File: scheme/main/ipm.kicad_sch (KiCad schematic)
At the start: 2 parts

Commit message: sheets titles
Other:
- title: (none) -> Силовой модуль
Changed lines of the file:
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@@
 	(generator_version "8.0")
 	(paper "A3")
+	(title_block
+		(title "Силовой модуль")
+	)
 	(junction
 		(at 205.74 96.52)

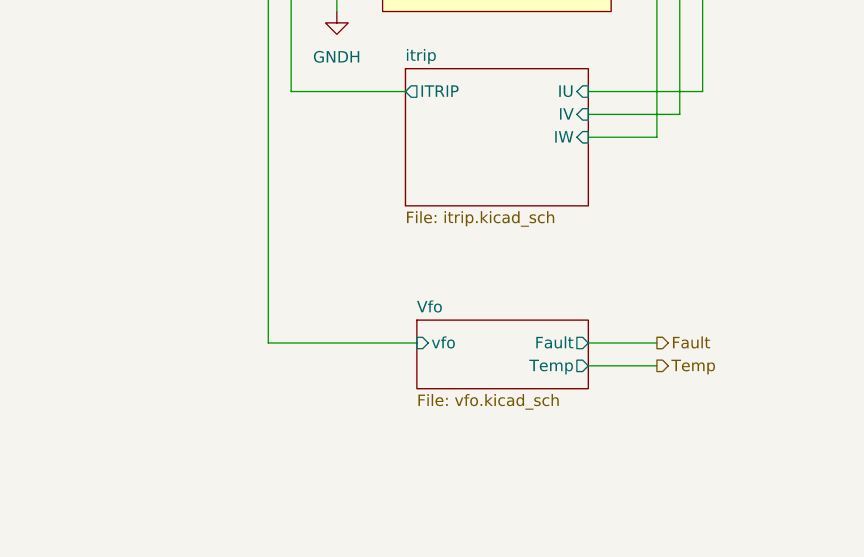
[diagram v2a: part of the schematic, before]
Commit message: vfo schematic separated to ipm_fault and ipm_temp & added rc filters
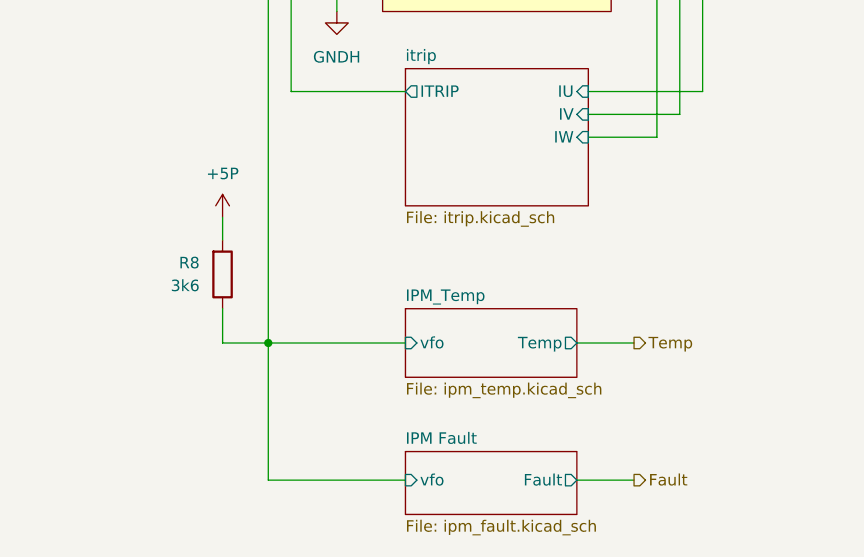
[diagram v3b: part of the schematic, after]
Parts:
- added R8: 3k6, Resistor_SMD:R_0805_2012Metric, symbol Device:R
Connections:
- net Vfo/vfo renamed IPM Fault/vfo
- net IPM Fault/vfo: now also R8.1
- new net +5P: R8.2
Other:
- removed sheet Vfo
- added sheet IPM Fault (ipm_fault.kicad_sch)
- added sheet IPM_Temp (ipm_temp.kicad_sch)

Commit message: fixed check errors
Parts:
- added F2: 8A, symbol Device:Fuse
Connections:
- net +VDC: now also F2.2; no longer C83.1, IPM1.23 (P)
- new net: C83.1, F2.1, IPM1.23 (P)
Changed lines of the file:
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@@
 	)
 	(junction
-		(at 205.74 96.52)
+		(at 215.9 96.52)
 		(diameter 0)
 		(color 0 0 0 0)
@@
 	(wire
 		(pts
-			(xy 205.74 91.44) (xy 205.74 96.52)
-		)
-		(stroke
-			(width 0)
-			(type default)
-		)
-	)
-	(wire
-		(pts
 			(xy 147.32 77.47) (xy 162.56 77.47)
 		)
@@
 	(wire
 		(pts
+			(xy 234.95 96.52) (xy 229.87 96.52)
+		)
+		(stroke
+			(width 0)
+			(type default)
+		)
+	)
+	(wire
+		(pts
 			(xy 170.18 137.16) (xy 160.02 137.16)
 		)
@@
 	(wire
 		(pts
+			(xy 234.95 93.98) (xy 234.95 96.52)
+		)
+		(stroke
+			(width 0)
+			(type default)
+		)
+	)
+	(wire
+		(pts
 			(xy 148.59 129.54) (xy 170.18 129.54)
 		)
@@
 		(pts
 			(xy 154.94 102.87) (xy 170.18 102.87)
+		)
+		(stroke
+			(width 0)
+			(type default)
+		)
+	)
+	(wire
+		(pts
+			(xy 215.9 96.52) (xy 222.25 96.52)
 		)
 		(stroke
@@
 	)
 	(symbol
+		(lib_id "Device:Fuse")
+		(at 226.06 96.52 90)
+		(unit 1)
+		(exclude_from_sim no)
+		(in_bom yes)
+		(on_board yes)
+		(dnp no)
+		(fields_autoplaced yes)
+		(property "Reference" "F2"
+			(at 226.06 90.17 90)
+			(effects
+				(font
+					(size 1.27 1.27)
+				)
+			)
+		)
+		(property "Value" "8A"
+			(at 226.06 92.71 90)
+			(effects
+				(font
+					(size 1.27 1.27)
+				)
+			)
+		)
+		(property "Footprint" ""
+			(at 226.06 98.298 90)
+			(effects
+				(font
+					(size 1.27 1.27)
+				)
+				(hide yes)
+			)
+		)
+		(property "Datasheet" "~"
+			(at 226.06 96.52 0)
+			(effects
+				(font
+					(size 1.27 1.27)
+				)
+				(hide yes)
+			)
+		)
+		(property "Description" "Fuse"
+			(at 226.06 96.52 0)
+			(effects
+				(font
+					(size 1.27 1.27)
+				)
+				(hide yes)
+			)
+		)
+		(pin "1"
+		)
+		(pin "2"
+		)
+		(instances
+			(project "main"
+				(path "/c11d1dbc-4db9-4712-8d1d-5f6f7086cded/5d407613-ca47-4478-86ea-137e1786be86"
+					(reference "F2")
+					(unit 1)
+				)
+			)
+		)
+	)
+	(symbol
 		(lib_id "main:GNDH")
 		(at 167.64 144.78 0)
@@
 	(symbol
 		(lib_id "power:+VDC")
-		(at 205.74 91.44 0)
+		(at 234.95 93.98 0)
 		(unit 1)
 		(exclude_from_sim no)
@@
 		(dnp no)
 		(fields_autoplaced yes)
-		(property "Reference" "#PWR2"
-			(at 205.74 93.98 0)
+		(property "Reference" "#PWR02"
+			(at 234.95 96.52 0)
 			(effects
 				(font
@@
 		)
 		(property "Value" "+VDC"
-			(at 205.74 83.82 0)
+			(at 234.95 86.36 0)
 			(effects
 				(font
@@
 		)
 		(property "Footprint" ""
-			(at 205.74 91.44 0)
+			(at 234.95 93.98 0)
 			(effects
 				(font
@@
 		)
 		(property "Datasheet" ""
-			(at 205.74 91.44 0)
+			(at 234.95 93.98 0)
 			(effects
 				(font
@@
 		)
 		(property "Description" "Power symbol creates a global label with name \"+VDC\""
-			(at 205.74 91.44 0)
+			(at 234.95 93.98 0)
 			(effects
 				(font
@@
 			(project "main"
 				(path "/c11d1dbc-4db9-4712-8d1d-5f6f7086cded/5d407613-ca47-4478-86ea-137e1786be86"
-					(reference "#PWR2")
+					(reference "#PWR02")
 					(unit 1)
 				)

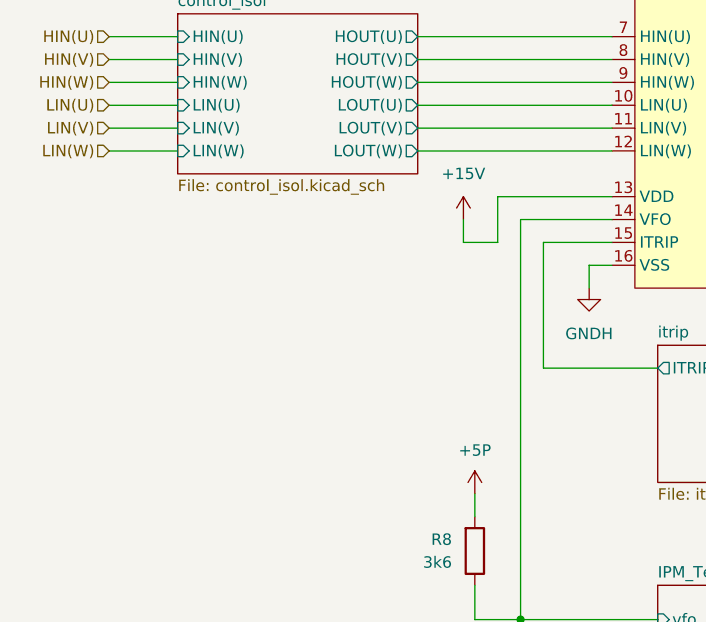
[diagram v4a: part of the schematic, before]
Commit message: added capacitors to ipm power supply pin && added zener 20V to ipm bootstrap and power pins
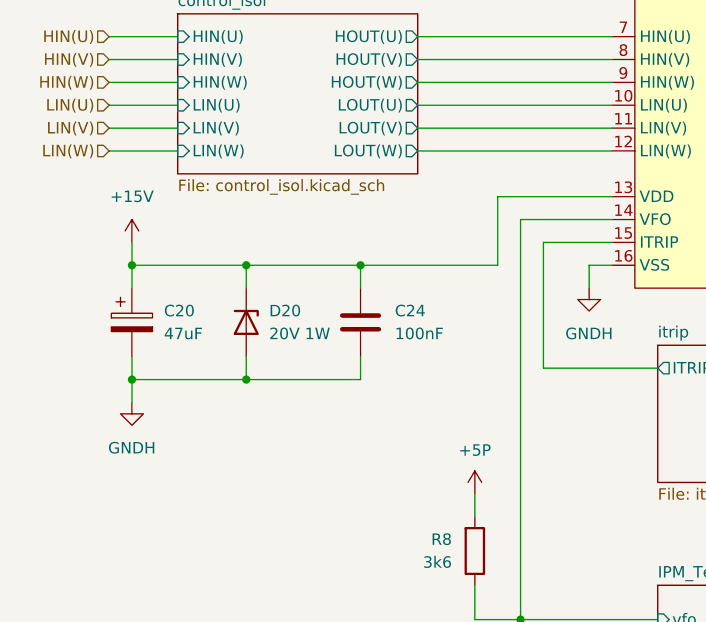
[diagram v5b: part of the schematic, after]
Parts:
- added C20: 47uF, Capacitor_SMD:C_Elec_5x5.8, symbol Device:C_Polarized
- added C24: 100nF, Capacitor_SMD:C_0805_2012Metric, symbol Device:C
- added D20: 20V 1W, symbol Device:D_Zener
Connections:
- net +15V: now also C20.1, C24.1, D20.1 (K)
- net GNDH: now also C20.2, C24.2, D20.2 (A)

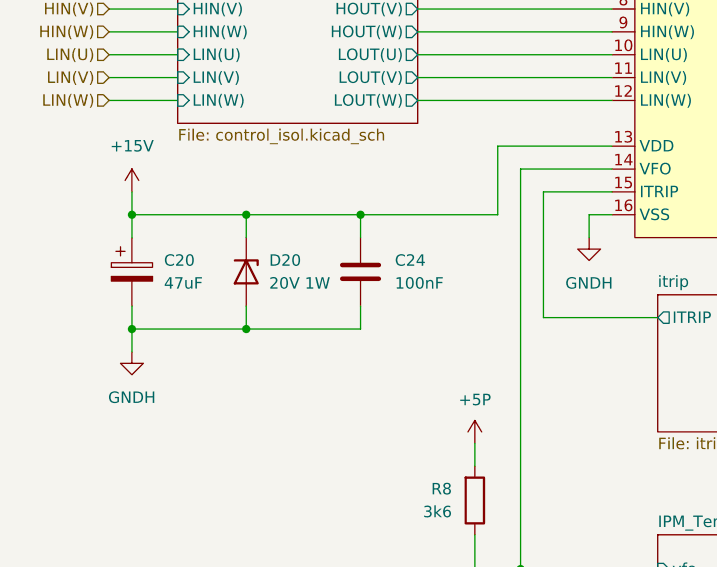
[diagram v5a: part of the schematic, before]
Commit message: footprints set/changed
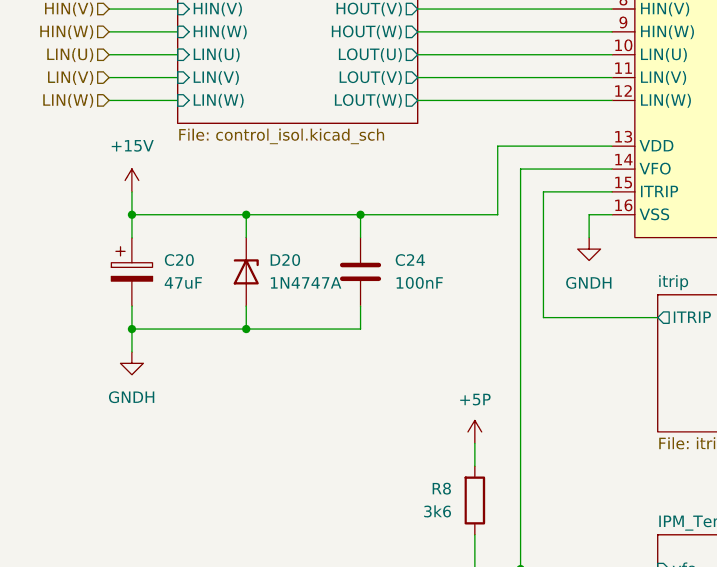
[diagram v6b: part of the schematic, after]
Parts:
- D20: value 20V 1W -> 1N4747A; footprint (none) -> Diode_THT:D_DO-41_SOD81_P10.16mm_Horizontal
- F2: footprint (none) -> main:Fuseholder_Clip-5x20mm_KLS5-266
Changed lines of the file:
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@@
 			)
 		)
-		(property "Value" "20V 1W"
+		(property "Value" "1N4747A"
 			(at 132.08 149.8599 90)
 			(effects
@@
 			)
 		)
-		(property "Footprint" ""
+		(property "Footprint" "Diode_THT:D_DO-41_SOD81_P10.16mm_Horizontal"
 			(at 129.54 148.59 0)
 			(effects
@@
 			)
 		)
-		(property "Description" "Zener diode"
+		(property "Description" "20V 1W"
 			(at 129.54 148.59 0)
 			(effects
@@
 			)
 		)
-		(property "Footprint" ""
+		(property "Footprint" "main:Fuseholder_Clip-5x20mm_KLS5-266"
 			(at 226.06 98.298 90)
 			(effects
